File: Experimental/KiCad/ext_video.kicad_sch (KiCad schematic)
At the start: 30 parts, among them IC13 RT9742SNGV, IC14 TPD4E001DRLR, IC15 TPD4E001DRLR, IC16 TPD12S016PWR, IC17 MIC2026A-1YM-TR, IC18 TPD4E001DRLR, X7 0862-1J1T-43-F, X8 SS-53000-002, X9 5051102091

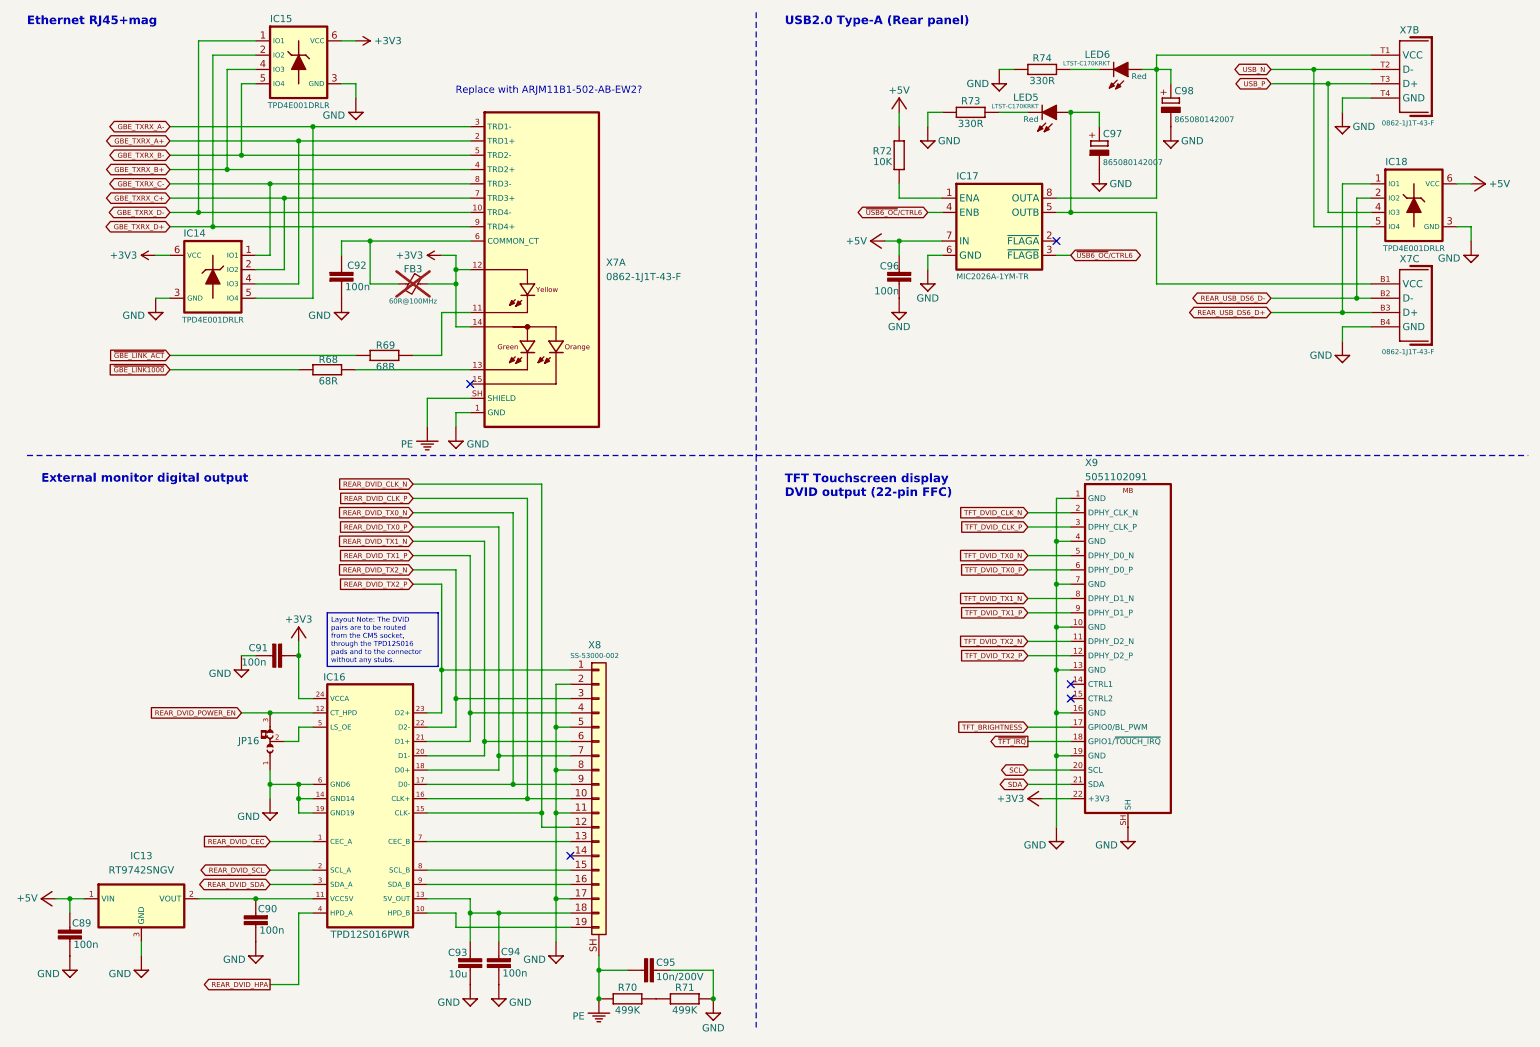
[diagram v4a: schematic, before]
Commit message: Output LC filters added on all buck converters
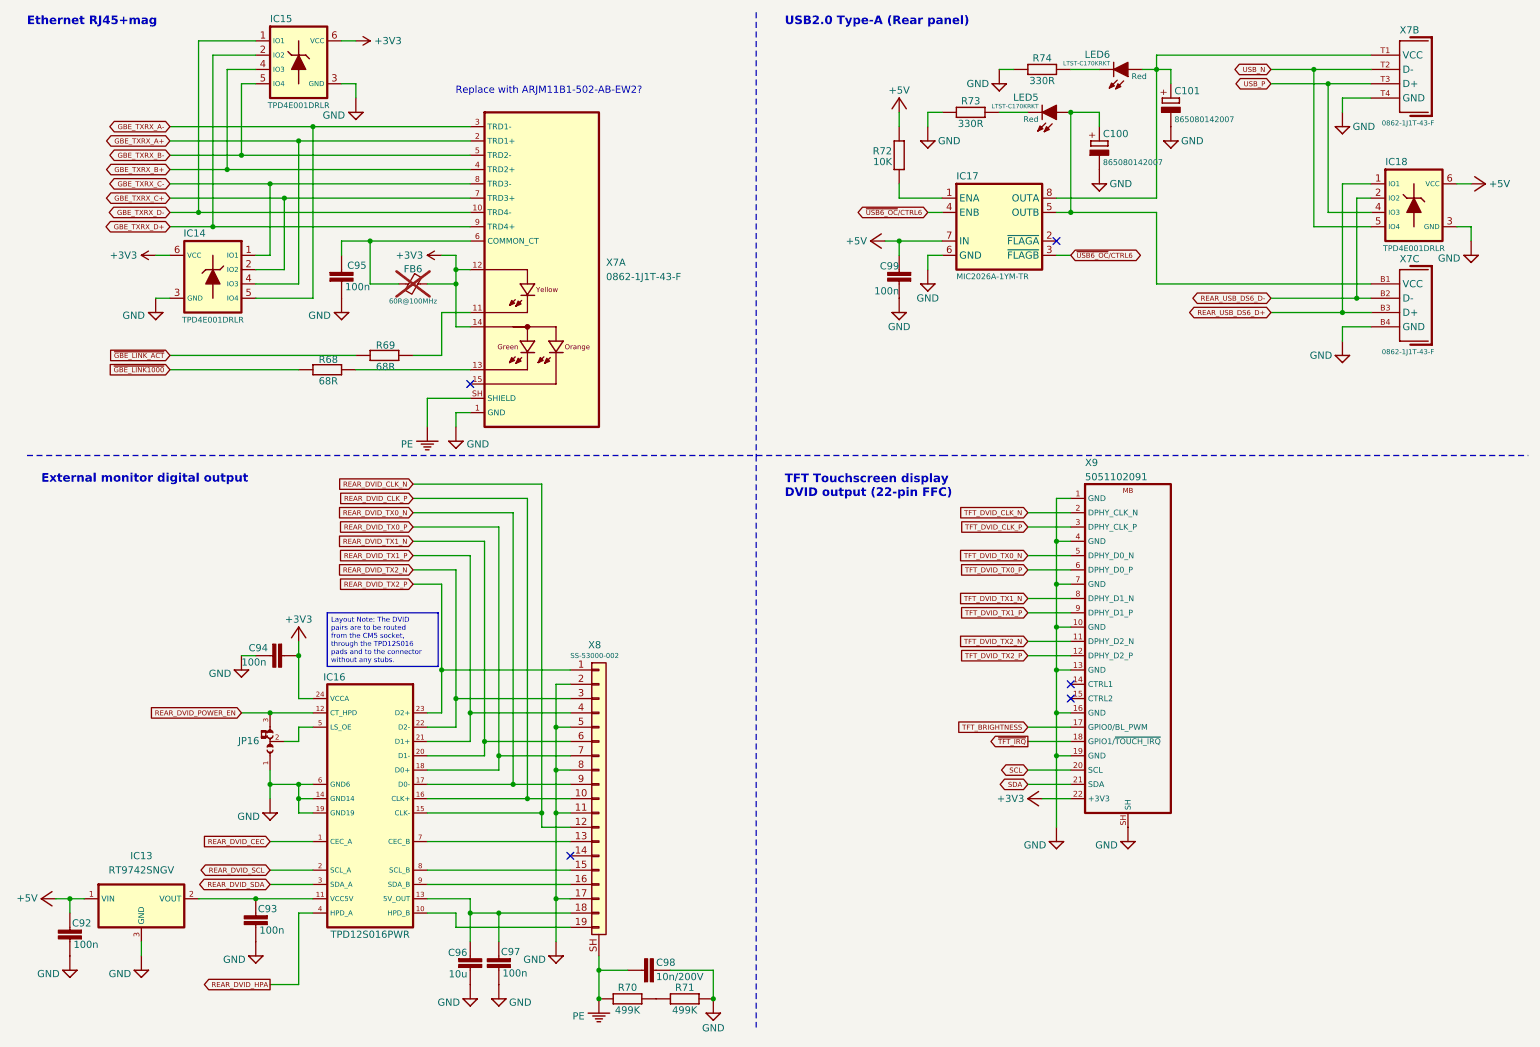
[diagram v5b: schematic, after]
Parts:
- renumbered C97 to C100, C98 to C101, C89 to C92, C90 to C93, C91 to C94, C92 to C95, C93 to C96, C94 to C97, C95 to C98, C96 to C99, FB3 to FB6
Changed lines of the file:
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@@
 	(title_block
 		(title "${project_name}")
-		(date "2025-10-13")
+		(date "2025-10-14")
 		(rev "${project_version}")
 		(company "${project_creator}")
@@
 		(on_board yes)
 		(dnp no)
-		(property "Reference" "#SUPPLY055"
+		(property "Reference" "#SUPPLY058"
 			(at 71.12 68.58 0)
 			(effects
@@
 			(project "BB3plus MCU test board"
 				(path "/1df84e4f-233a-4f72-9418-c0020706bb76/c0a485a3-023d-4313-ae06-c16e1fdbf75a"
-					(reference "#SUPPLY055")
+					(reference "#SUPPLY058")
 					(unit 1)
 				)
@@
 		(on_board yes)
 		(dnp no)
-		(property "Reference" "C91"
+		(property "Reference" "C94"
 			(at 54.61 128.905 90)
 			(effects
@@
 			(project "BB3plus MCU test board"
 				(path "/1df84e4f-233a-4f72-9418-c0020706bb76/c0a485a3-023d-4313-ae06-c16e1fdbf75a"
-					(reference "C91")
+					(reference "C94")
 					(unit 1)
 				)
@@
 		(on_board yes)
 		(dnp no)
-		(property "Reference" "C97"
+		(property "Reference" "C100"
 			(at 206.375 36.83 0)
 			(effects
@@
 			(project "BB3plus MCU test board"
 				(path "/1df84e4f-233a-4f72-9418-c0020706bb76/c0a485a3-023d-4313-ae06-c16e1fdbf75a"
-					(reference "C97")
+					(reference "C100")
 					(unit 1)
 				)
@@
 		(on_board yes)
 		(dnp no)
-		(property "Reference" "#SUPPLY054"
+		(property "Reference" "#SUPPLY057"
 			(at 38.1 68.58 0)
 			(effects
@@
 			(project "BB3plus MCU test board"
 				(path "/1df84e4f-233a-4f72-9418-c0020706bb76/c0a485a3-023d-4313-ae06-c16e1fdbf75a"
-					(reference "#SUPPLY054")
+					(reference "#SUPPLY057")
 					(unit 1)
 				)
@@
 		(on_board yes)
 		(dnp yes)
-		(property "Reference" "FB3"
+		(property "Reference" "FB6"
 			(at 83.82 61.595 90)
 			(effects
@@
 			(project "BB3plus MCU test board"
 				(path "/1df84e4f-233a-4f72-9418-c0020706bb76/c0a485a3-023d-4313-ae06-c16e1fdbf75a"
-					(reference "FB3")
+					(reference "FB6")
 					(unit 1)
 				)
@@
 		(on_board yes)
 		(dnp no)
-		(property "Reference" "C89"
+		(property "Reference" "C92"
 			(at 26.67 177.8 0)
 			(effects
@@
 			(project "BB3plus MCU test board"
 				(path "/1df84e4f-233a-4f72-9418-c0020706bb76/c0a485a3-023d-4313-ae06-c16e1fdbf75a"
-					(reference "C89")
+					(reference "C92")
 					(unit 1)
 				)
@@
 		(on_board yes)
 		(dnp no)
-		(property "Reference" "#SUPPLY058"
+		(property "Reference" "#SUPPLY061"
 			(at 271.78 58.42 0)
 			(effects
@@
 			(project "BB3plus MCU test board"
 				(path "/1df84e4f-233a-4f72-9418-c0020706bb76/c0a485a3-023d-4313-ae06-c16e1fdbf75a"
-					(reference "#SUPPLY058")
+					(reference "#SUPPLY061")
 					(unit 1)
 				)
@@
 		(on_board yes)
 		(dnp no)
-		(property "Reference" "C93"
+		(property "Reference" "C96"
 			(at 93.472 183.0324 0)
 			(effects
@@
 			(project "BB3plus MCU test board"
 				(path "/1df84e4f-233a-4f72-9418-c0020706bb76/c0a485a3-023d-4313-ae06-c16e1fdbf75a"
-					(reference "C93")
+					(reference "C96")
 					(unit 1)
 				)
@@
 		(on_board yes)
 		(dnp no)
-		(property "Reference" "#SUPPLY057"
+		(property "Reference" "#SUPPLY060"
 			(at 91.44 91.44 0)
 			(effects
@@
 			(project "BB3plus MCU test board"
 				(path "/1df84e4f-233a-4f72-9418-c0020706bb76/c0a485a3-023d-4313-ae06-c16e1fdbf75a"
-					(reference "#SUPPLY057")
+					(reference "#SUPPLY060")
 					(unit 1)
 				)
@@
 		(on_board yes)
 		(dnp no)
-		(property "Reference" "C94"
+		(property "Reference" "C97"
 			(at 102.87 182.88 0)
 			(effects
@@
 			(project "BB3plus MCU test board"
 				(path "/1df84e4f-233a-4f72-9418-c0020706bb76/c0a485a3-023d-4313-ae06-c16e1fdbf75a"
-					(reference "C94")
+					(reference "C97")
 					(unit 1)
 				)
@@
 		(on_board yes)
 		(dnp no)
-		(property "Reference" "C90"
+		(property "Reference" "C93"
 			(at 59.69 175.26 0)
 			(effects
@@
 			(project "BB3plus MCU test board"
 				(path "/1df84e4f-233a-4f72-9418-c0020706bb76/c0a485a3-023d-4313-ae06-c16e1fdbf75a"
-					(reference "C90")
+					(reference "C93")
 					(unit 1)
 				)
@@
 		(on_board yes)
 		(dnp no)
-		(property "Reference" "C92"
+		(property "Reference" "C95"
 			(at 75.565 60.96 0)
 			(effects
@@
 			(project "BB3plus MCU test board"
 				(path "/1df84e4f-233a-4f72-9418-c0020706bb76/c0a485a3-023d-4313-ae06-c16e1fdbf75a"
-					(reference "C92")
+					(reference "C95")
 					(unit 1)
 				)
@@
 		(on_board yes)
 		(dnp no)
-		(property "Reference" "C96"
+		(property "Reference" "C99"
 			(at 170.18 60.325 0)
 			(effects
@@
 			(project "BB3plus MCU test board"
 				(path "/1df84e4f-233a-4f72-9418-c0020706bb76/c0a485a3-023d-4313-ae06-c16e1fdbf75a"
-					(reference "C96")
+					(reference "C99")
 					(unit 1)
 				)
@@
 		(on_board yes)
 		(dnp no)
-		(property "Reference" "C95"
+		(property "Reference" "C98"
 			(at 127 184.785 90)
 			(effects
@@
 			(project "BB3plus MCU test board"
 				(path "/1df84e4f-233a-4f72-9418-c0020706bb76/c0a485a3-023d-4313-ae06-c16e1fdbf75a"
-					(reference "C95")
+					(reference "C98")
 					(unit 1)
 				)
@@
 		(on_board yes)
 		(dnp no)
-		(property "Reference" "C98"
+		(property "Reference" "C101"
 			(at 219.075 29.21 0)
 			(effects
@@
 			(project "BB3plus MCU test board"
 				(path "/1df84e4f-233a-4f72-9418-c0020706bb76/c0a485a3-023d-4313-ae06-c16e1fdbf75a"
-					(reference "C98")
+					(reference "C101")
 					(unit 1)
 				)
@@
 		(on_board yes)
 		(dnp no)
-		(property "Reference" "#SUPPLY056"
+		(property "Reference" "#SUPPLY059"
 			(at 73.66 33.02 0)
 			(effects
@@
 			(project "BB3plus MCU test board"
 				(path "/1df84e4f-233a-4f72-9418-c0020706bb76/c0a485a3-023d-4313-ae06-c16e1fdbf75a"
-					(reference "#SUPPLY056")
+					(reference "#SUPPLY059")
 					(unit 1)
 				)

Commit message: Various small fixes
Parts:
- renumbered LED5 to LED6, LED6 to LED7, R68 to R69, R69 to R70, R70 to R71, R71 to R72, R72 to R73, R73 to R74, R74 to R75
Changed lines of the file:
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@@
 		(on_board yes)
 		(dnp no)
-		(property "Reference" "R74"
+		(property "Reference" "R75"
 			(at 195.58 24.13 90)
 			(effects
@@
 			(project "BB3plus MCU test board"
 				(path "/1df84e4f-233a-4f72-9418-c0020706bb76/c0a485a3-023d-4313-ae06-c16e1fdbf75a"
-					(reference "R74")
+					(reference "R75")
 					(unit 1)
 				)
@@
 		(on_board yes)
 		(dnp no)
-		(property "Reference" "#SUPPLY058"
+		(property "Reference" "#SUPPLY059"
 			(at 71.12 68.58 0)
 			(effects
@@
 			(project "BB3plus MCU test board"
 				(path "/1df84e4f-233a-4f72-9418-c0020706bb76/c0a485a3-023d-4313-ae06-c16e1fdbf75a"
-					(reference "#SUPPLY058")
+					(reference "#SUPPLY059")
 					(unit 1)
 				)
@@
 		(on_board yes)
 		(dnp no)
-		(property "Reference" "R73"
+		(property "Reference" "R74"
 			(at 182.88 31.75 90)
 			(effects
@@
 			(project "BB3plus MCU test board"
 				(path "/1df84e4f-233a-4f72-9418-c0020706bb76/c0a485a3-023d-4313-ae06-c16e1fdbf75a"
-					(reference "R73")
+					(reference "R74")
 					(unit 1)
 				)
@@
 		(on_board yes)
 		(dnp no)
-		(property "Reference" "#SUPPLY057"
+		(property "Reference" "#SUPPLY058"
 			(at 38.1 68.58 0)
 			(effects
@@
 			(project "BB3plus MCU test board"
 				(path "/1df84e4f-233a-4f72-9418-c0020706bb76/c0a485a3-023d-4313-ae06-c16e1fdbf75a"
-					(reference "#SUPPLY057")
+					(reference "#SUPPLY058")
 					(unit 1)
 				)
@@
 		(on_board yes)
 		(dnp no)
-		(property "Reference" "R72"
+		(property "Reference" "R73"
 			(at 168.91 40.64 0)
 			(effects
@@
 			(project "BB3plus MCU test board"
 				(path "/1df84e4f-233a-4f72-9418-c0020706bb76/c0a485a3-023d-4313-ae06-c16e1fdbf75a"
-					(reference "R72")
+					(reference "R73")
 					(unit 1)
 				)
@@
 		(on_board yes)
 		(dnp no)
-		(property "Reference" "LED6"
+		(property "Reference" "LED7"
 			(at 207.645 23.495 90)
 			(effects
@@
 			(project "BB3plus MCU test board"
 				(path "/1df84e4f-233a-4f72-9418-c0020706bb76/c0a485a3-023d-4313-ae06-c16e1fdbf75a"
-					(reference "LED6")
+					(reference "LED7")
 					(unit 1)
 				)
@@
 		(on_board yes)
 		(dnp no)
-		(property "Reference" "R71"
+		(property "Reference" "R72"
 			(at 132.08 189.23 90)
 			(effects
@@
 			(project "BB3plus MCU test board"
 				(path "/1df84e4f-233a-4f72-9418-c0020706bb76/c0a485a3-023d-4313-ae06-c16e1fdbf75a"
-					(reference "R71")
+					(reference "R72")
 					(unit 1)
 				)
@@
 		(on_board yes)
 		(dnp no)
-		(property "Reference" "#SUPPLY061"
+		(property "Reference" "#SUPPLY062"
 			(at 271.78 58.42 0)
 			(effects
@@
 			(project "BB3plus MCU test board"
 				(path "/1df84e4f-233a-4f72-9418-c0020706bb76/c0a485a3-023d-4313-ae06-c16e1fdbf75a"
-					(reference "#SUPPLY061")
+					(reference "#SUPPLY062")
 					(unit 1)
 				)
@@
 		(on_board yes)
 		(dnp no)
-		(property "Reference" "R68"
+		(property "Reference" "R69"
 			(at 70.485 76.2 90)
 			(effects
@@
 			(project "BB3plus MCU test board"
 				(path "/1df84e4f-233a-4f72-9418-c0020706bb76/c0a485a3-023d-4313-ae06-c16e1fdbf75a"
-					(reference "R68")
+					(reference "R69")
 					(unit 1)
 				)
@@
 		(on_board yes)
 		(dnp no)
-		(property "Reference" "#SUPPLY060"
+		(property "Reference" "#SUPPLY061"
 			(at 91.44 91.44 0)
 			(effects
@@
 			(project "BB3plus MCU test board"
 				(path "/1df84e4f-233a-4f72-9418-c0020706bb76/c0a485a3-023d-4313-ae06-c16e1fdbf75a"
-					(reference "#SUPPLY060")
+					(reference "#SUPPLY061")
 					(unit 1)
 				)
@@
 		(on_board yes)
 		(dnp no)
-		(property "Reference" "R70"
+		(property "Reference" "R71"
 			(at 121.92 189.23 90)
 			(effects
@@
 			(project "BB3plus MCU test board"
 				(path "/1df84e4f-233a-4f72-9418-c0020706bb76/c0a485a3-023d-4313-ae06-c16e1fdbf75a"
-					(reference "R70")
+					(reference "R71")
 					(unit 1)
 				)
@@
 		(on_board yes)
 		(dnp no)
-		(property "Reference" "R69"
+		(property "Reference" "R70"
 			(at 80.645 73.66 90)
 			(effects
@@
 			(project "BB3plus MCU test board"
 				(path "/1df84e4f-233a-4f72-9418-c0020706bb76/c0a485a3-023d-4313-ae06-c16e1fdbf75a"
-					(reference "R69")
+					(reference "R70")
 					(unit 1)
 				)
@@
 		(on_board yes)
 		(dnp no)
-		(property "Reference" "LED5"
+		(property "Reference" "LED6"
 			(at 194.945 31.115 90)
 			(effects
@@
 			(project "BB3plus MCU test board"
 				(path "/1df84e4f-233a-4f72-9418-c0020706bb76/c0a485a3-023d-4313-ae06-c16e1fdbf75a"
-					(reference "LED5")
+					(reference "LED6")
 					(unit 1)
 				)
@@
 		(on_board yes)
 		(dnp no)
-		(property "Reference" "#SUPPLY059"
+		(property "Reference" "#SUPPLY060"
 			(at 73.66 33.02 0)
 			(effects
@@
 			(project "BB3plus MCU test board"
 				(path "/1df84e4f-233a-4f72-9418-c0020706bb76/c0a485a3-023d-4313-ae06-c16e1fdbf75a"
-					(reference "#SUPPLY059")
+					(reference "#SUPPLY060")
 					(unit 1)
 				)

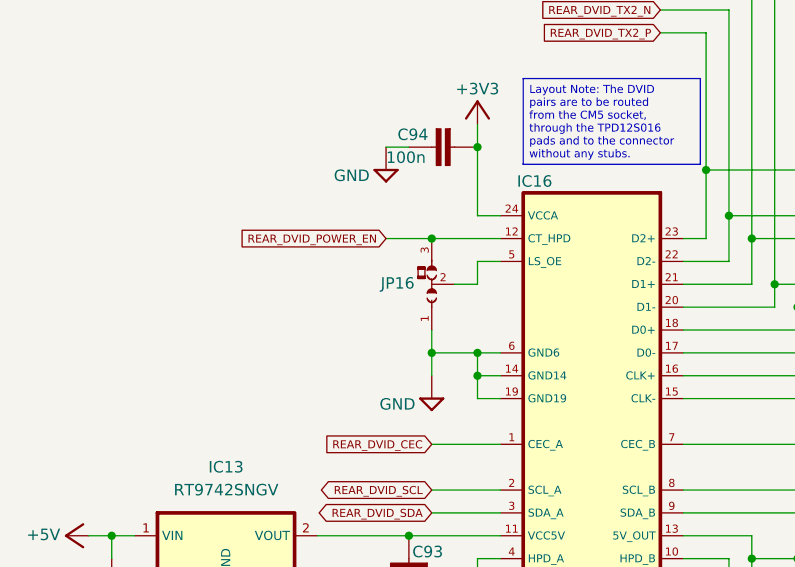
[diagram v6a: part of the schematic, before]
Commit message: Hub section corrections in collaboration with Microchip support
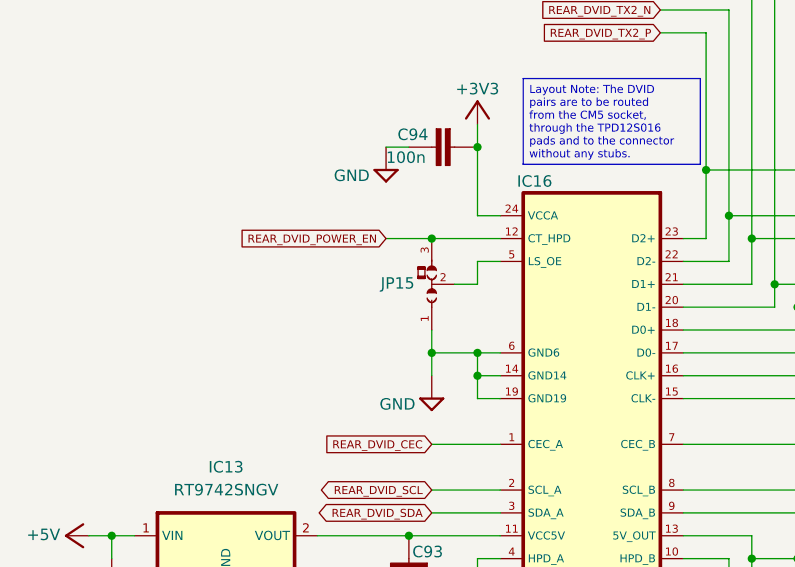
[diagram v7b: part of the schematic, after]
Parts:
- renumbered JP16 to JP15
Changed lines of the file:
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@@
 	(title_block
 		(title "${project_name}")
-		(date "2025-10-14")
+		(date "2025-10-15")
 		(rev "${project_version}")
 		(company "${project_creator}")
@@
 		(on_board yes)
 		(dnp no)
-		(property "Reference" "#+3V026"
+		(property "Reference" "#+3V027"
 			(at 193.04 154.94 0)
 			(effects
@@
 			(project "BB3plus MCU test board"
 				(path "/1df84e4f-233a-4f72-9418-c0020706bb76/c0a485a3-023d-4313-ae06-c16e1fdbf75a"
-					(reference "#+3V026")
+					(reference "#+3V027")
 					(unit 1)
 				)
@@
 		(on_board yes)
 		(dnp no)
-		(property "Reference" "#PWR033"
+		(property "Reference" "#PWR034"
 			(at 92.71 58.42 0)
 			(effects
@@
 			(project "BB3plus MCU test board"
 				(path "/1df84e4f-233a-4f72-9418-c0020706bb76/c0a485a3-023d-4313-ae06-c16e1fdbf75a"
-					(reference "#PWR033")
+					(reference "#PWR034")
 					(unit 1)
 				)
@@
 		(on_board yes)
 		(dnp no)
-		(property "Reference" "#PWR031"
+		(property "Reference" "#PWR032"
 			(at 41.91 58.42 0)
 			(effects
@@
 			(project "BB3plus MCU test board"
 				(path "/1df84e4f-233a-4f72-9418-c0020706bb76/c0a485a3-023d-4313-ae06-c16e1fdbf75a"
-					(reference "#PWR031")
+					(reference "#PWR032")
 					(unit 1)
 				)
@@
 		(on_board yes)
 		(dnp no)
-		(property "Reference" "#PWR032"
+		(property "Reference" "#PWR033"
 			(at 69.85 20.32 0)
 			(effects
@@
 			(project "BB3plus MCU test board"
 				(path "/1df84e4f-233a-4f72-9418-c0020706bb76/c0a485a3-023d-4313-ae06-c16e1fdbf75a"
-					(reference "#PWR032")
+					(reference "#PWR033")
 					(unit 1)
 				)
@@
 		(on_board yes)
 		(dnp no)
-		(property "Reference" "#+3V025"
+		(property "Reference" "#+3V026"
 			(at 63.5 124.46 0)
 			(effects
@@
 			(project "BB3plus MCU test board"
 				(path "/1df84e4f-233a-4f72-9418-c0020706bb76/c0a485a3-023d-4313-ae06-c16e1fdbf75a"
-					(reference "#+3V025")
+					(reference "#+3V026")
 					(unit 1)
 				)
@@
 		(on_board yes)
 		(dnp no)
-		(property "Reference" "JP16"
+		(property "Reference" "JP15"
 			(at 56.515 145.415 90)
 			(effects
@@
 			(project "BB3plus MCU test board"
 				(path "/1df84e4f-233a-4f72-9418-c0020706bb76/c0a485a3-023d-4313-ae06-c16e1fdbf75a"
-					(reference "JP16")
+					(reference "JP15")
 					(unit 1)
 				)
